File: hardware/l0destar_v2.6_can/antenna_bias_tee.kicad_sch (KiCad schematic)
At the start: 11 parts

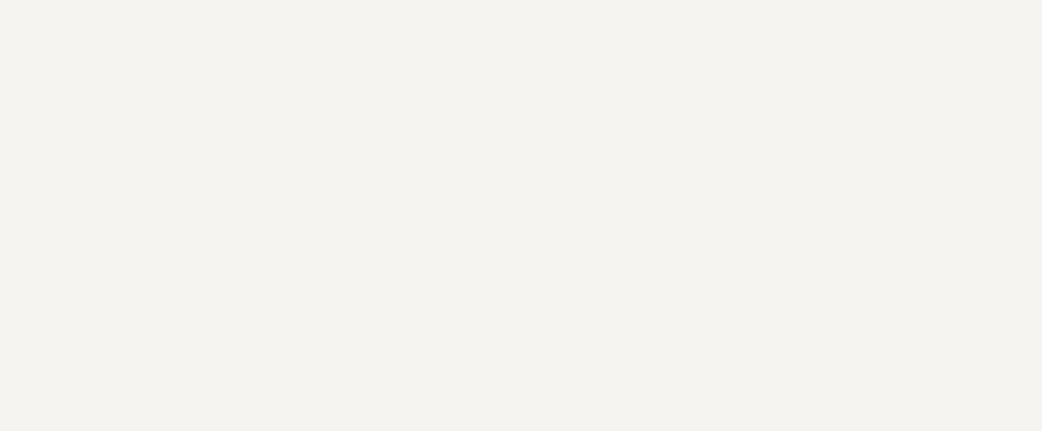
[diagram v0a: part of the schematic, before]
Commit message: fix sheet annotations
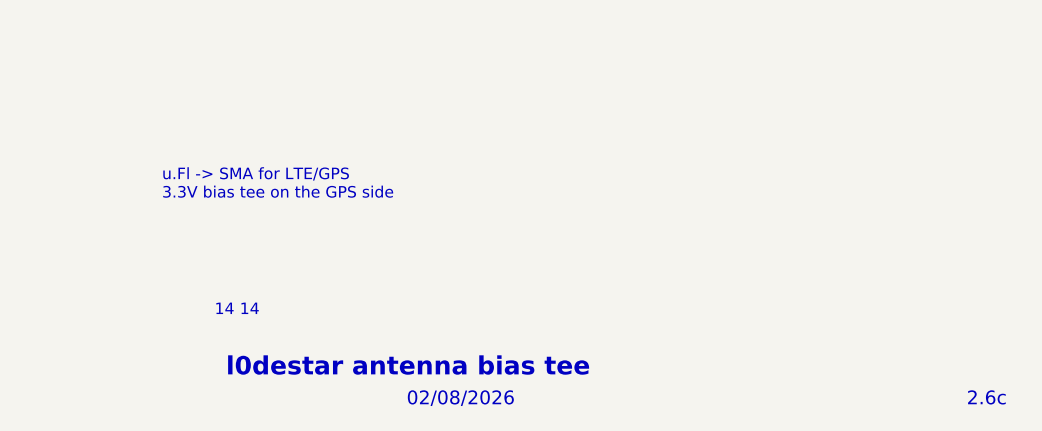
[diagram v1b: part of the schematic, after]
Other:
- note added: "02/08/2026"
- note added: "14"
- note added: "2.6c"
- note added: "l0destar antenna bias tee"
- note added: "u.Fl -> SMA for LTE/GPS 3.3V bias tee on the GPS side"
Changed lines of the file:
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@@
 	(generator_version "10.0")
 	(paper "A4")
+	(text "l0destar antenna bias tee"
+		(exclude_from_sim no)
+		(at 186.182 189.865 0)
+		(effects
+			(font
+				(face "KiCad Font")
+				(size 2.032 2.032)
+				(thickness 0.4064)
+				(bold yes)
+			)
+			(justify left)
+		)
+	)
+	(text "02/08/2026"
+		(exclude_from_sim no)
+		(at 206.248 193.421 0)
+		(effects
+			(font
+				(face "KiCad Font")
+				(size 1.524 1.524)
+				(thickness 0.1905)
+			)
+			(justify left)
+		)
+	)
+	(text "14"
+		(exclude_from_sim no)
+		(at 187.706 183.515 0)
+		(effects
+			(font
+				(size 1.27 1.27)
+			)
+			(justify left)
+		)
+	)
+	(text "14"
+		(exclude_from_sim no)
+		(at 184.912 183.515 0)
+		(effects
+			(font
+				(size 1.27 1.27)
+			)
+			(justify left)
+		)
+	)
+	(text "u.Fl -> SMA for LTE/GPS\n3.3V bias tee on the GPS side"
+		(exclude_from_sim no)
+		(at 179.07 169.545 0)
+		(effects
+			(font
+				(size 1.27 1.27)
+			)
+			(justify left)
+		)
+	)
+	(text "2.6c"
+		(exclude_from_sim no)
+		(at 268.478 193.421 0)
+		(effects
+			(font
+				(face "KiCad Font")
+				(size 1.524 1.524)
+				(thickness 0.1905)
+			)
+			(justify left)
+		)
+	)
 	(junction
 		(at 149.86 50.8)
